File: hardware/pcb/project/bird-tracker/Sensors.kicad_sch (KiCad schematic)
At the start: 2 parts, among them U4 LSM6DS3TR, U5 STTS22HTR

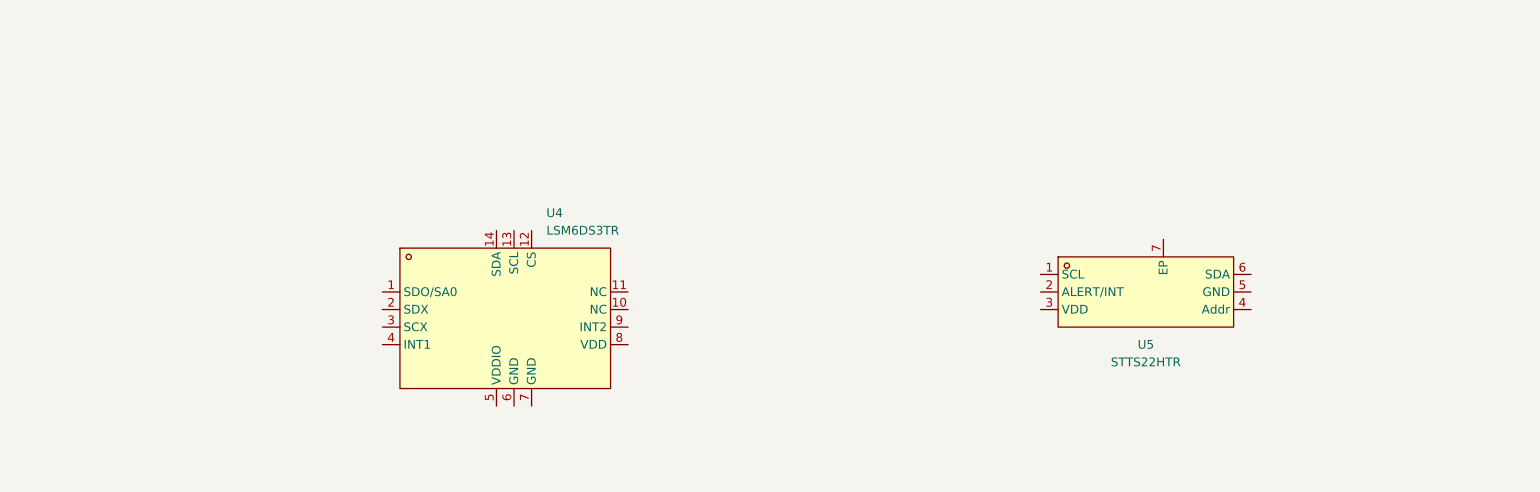
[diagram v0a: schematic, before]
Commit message: Sensors sheet complete
Revision v0.1
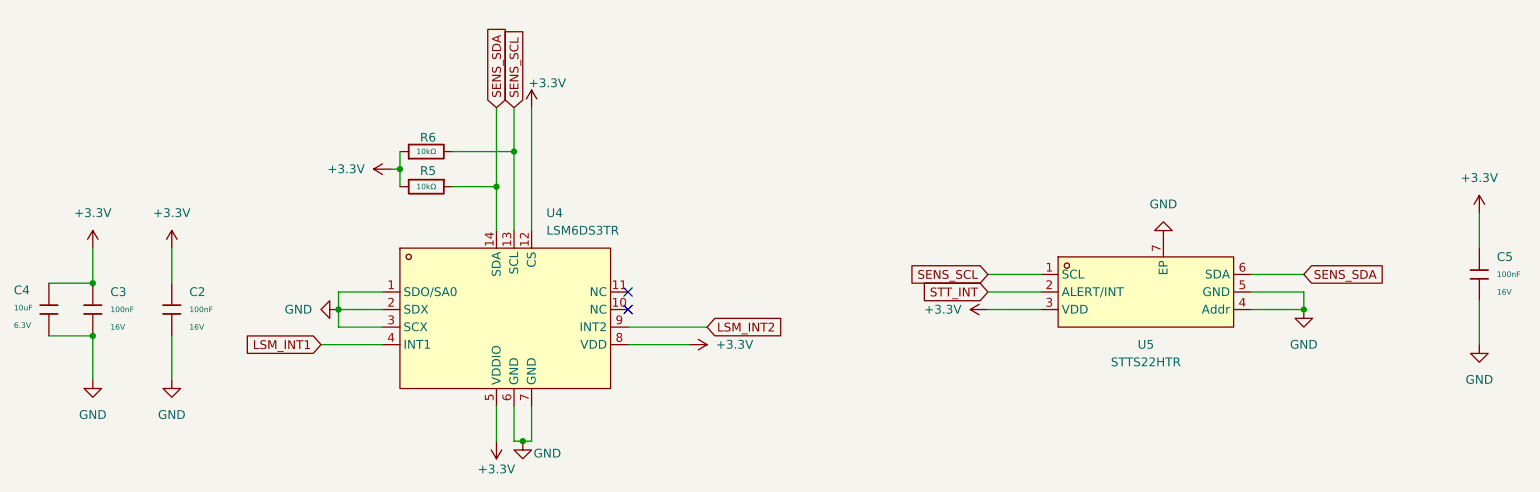
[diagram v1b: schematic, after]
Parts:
- added C2, C3, C5: 100nF, PCM_JLCPCB:C_0402, symbol PCM_JLCPCB-Capacitors:0402,100nF
- added C4: 10uF, PCM_JLCPCB:C_0402, symbol PCM_JLCPCB-Capacitors:0402,10uF
- added R5, R6: 10kΩ, PCM_JLCPCB:R_0402, symbol PCM_JLCPCB-Resistors:0402,10kΩ
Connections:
- net GND: now reaches U4.1 (SDO/SA0)
- net GND: now also U4.2 (SDX), U4.3 (SCX), U4.6 (GND), U4.7 (GND), U5.4 (Addr), U5.5 (GND), U5.7 (EP), C2.2, C3.2, C4.2, C5.2
- net +3.3V: now reaches U4.12 (CS)
- net +3.3V: now also U4.5 (VDDIO), U4.8 (VDD), U5.3 (VDD), C2.1, C3.1, C4.1, C5.1, R5.2, R6.1
- net SENS_SCL: now reaches U4.13 (SCL)
- net SENS_SCL: now also U5.1 (SCL), R6.2
- net SENS_SDA: now reaches U4.14 (SDA)
- net SENS_SDA: now also U5.6 (SDA), R5.1
- net LSM_INT1: now reaches U4.4 (INT1)
- net LSM_INT2: now reaches U4.9 (INT2)
- net STT_INT: now reaches U5.2 (ALERT/INT)
- no-connect marks 0 -> 2
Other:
- title: (none) -> Bird Tracker - Sensors
